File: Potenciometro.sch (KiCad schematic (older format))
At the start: 1 part

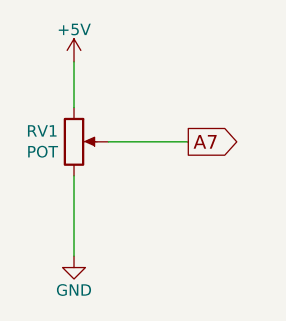
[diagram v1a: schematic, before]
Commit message: cambiar ch340T por ch340g y añadir nc a pines
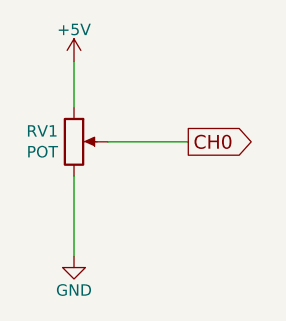
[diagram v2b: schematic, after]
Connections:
- net A7 renamed CH0
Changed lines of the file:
@@
 $Descr User 8268 5846
 encoding utf-8
-Sheet 14 15
+Sheet 13 14
 Title "Potenciometro"
 Date "2017-01-25"
@@
 $EndDescr
 $Comp
-L +5V #PWR0119
+L +5V #PWR0127
 U 1 1 588EB910
 P 2550 2150
-F 0 "#PWR0119" H 2550 2000 50  0001 C CNN
+F 0 "#PWR0127" H 2550 2000 50  0001 C CNN
 F 1 "+5V" H 2550 2290 50  0000 C CNN
 F 2 "" H 2550 2150 50  0000 C CNN
@@
 $EndComp
 $Comp
-L GND #PWR0120
+L GND #PWR0128
 U 1 1 588EB911
 P 2550 3000
-F 0 "#PWR0120" H 2550 2750 50  0001 C CNN
+F 0 "#PWR0128" H 2550 2750 50  0001 C CNN
 F 1 "GND" H 2550 2850 50  0000 C CNN
 F 2 "" H 2550 3000 50  0000 C CNN
@@
 	2550 3000 2550 2650
 Text GLabel 3050 2500 2    60   Output ~ 0
-A7
+CH0
 $Bitmap
 Pos 7500 4400
